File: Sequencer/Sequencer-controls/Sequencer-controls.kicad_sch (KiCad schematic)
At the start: 10 parts, among them SW1 SW_Push_DPDT, SW2 SW_Rotary3x4, SW3 SW_Rotary12

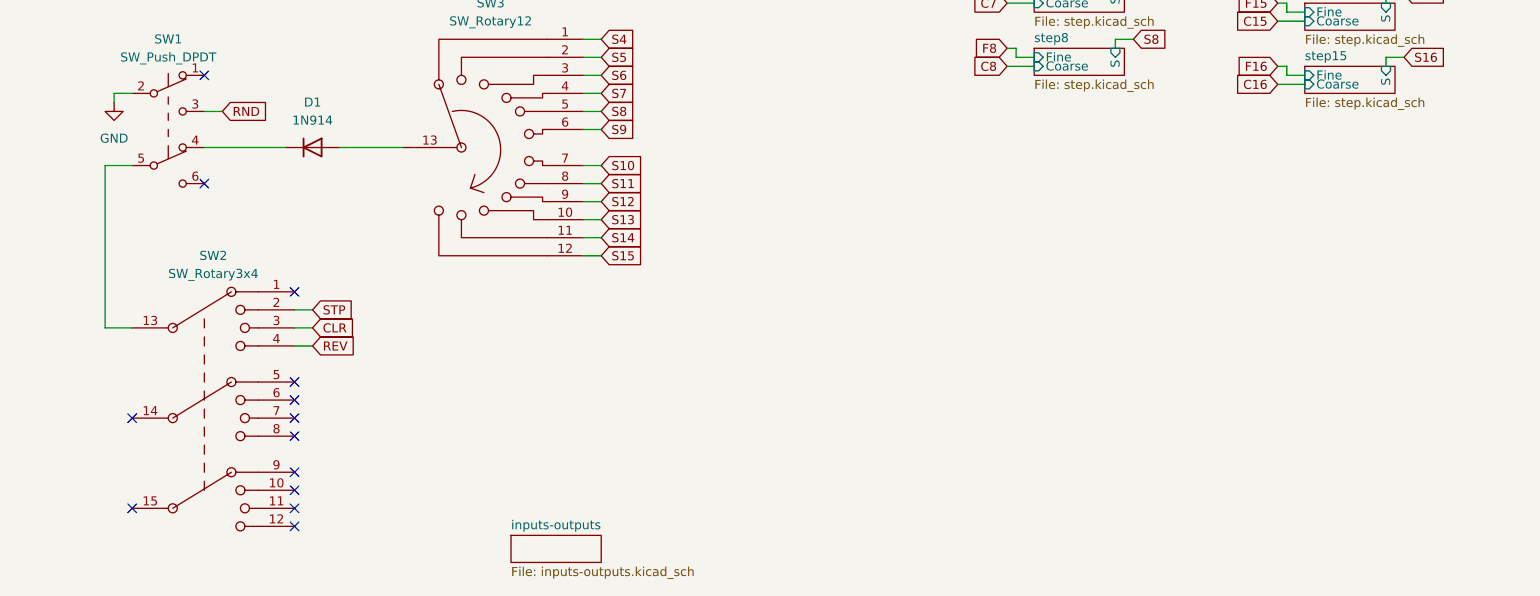
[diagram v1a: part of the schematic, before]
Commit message: adding connectors to sequencer
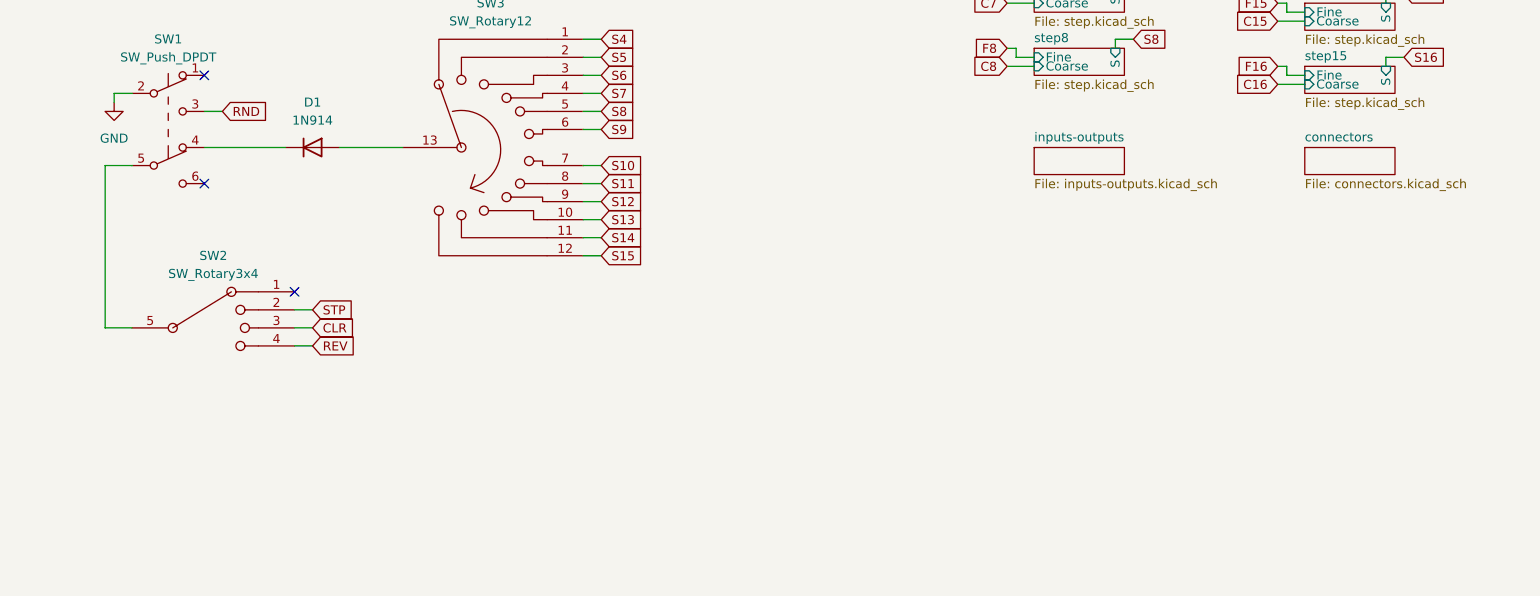
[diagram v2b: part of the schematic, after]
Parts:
- SW2: footprint (none) -> Library:rotary_switch_1P12T; symbol Switch:SW_Rotary3x4 -> Synth:SW_Rotary4
- SW3: footprint (none) -> Library:rotary_switch_1P12T
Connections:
- net at SW1.5 (B): now also SW2.5; no longer SW2.13
- no-connect marks 13 -> 3
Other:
- added sheet connectors (connectors.kicad_sch)
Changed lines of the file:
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@@
   )
   (no_connect (at 99.06 91.44))
-  (no_connect (at 88.9 139.7))
-  (no_connect (at 111.76 154.94))
-  (no_connect (at 88.9 152.4))
   (no_connect (at 111.76 121.92))
   (no_connect (at 99.06 106.68))
-  (no_connect (at 111.76 149.86))
-  (no_connect (at 111.76 142.24))
-  (no_connect (at 111.76 134.62))
-  (no_connect (at 111.76 139.7))
-  (no_connect (at 111.76 137.16))
-  (no_connect (at 111.76 152.4))
-  (no_connect (at 111.76 147.32))
   (wire (pts (xy 251.46 52.07) (xy 250.19 52.07))
     (stroke (width 0) (type default))
@@
       (effects (font (size 1.27 1.27)))
     )
-    (property "Footprint" "" (at 137.16 83.82 0)
+    (property "Footprint" "Library:rotary_switch_1P12T" (at 137.16 83.82 0)
       (effects (font (size 1.27 1.27)) hide)
     )
@@
     )
   )
-  (symbol (lib_id "Switch:SW_Rotary3x4") (at 99.06 139.7 0) (unit 1)
-    (in_bom yes) (on_board no) (dnp no) (fields_autoplaced)
+  (symbol (lib_id "Synth:SW_Rotary4") (at 99.06 127 0) (unit 1)
+    (in_bom yes) (on_board yes) (dnp no) (fields_autoplaced)
     (property "Reference" "SW2" (at 100.33 116.84 0)
       (effects (font (size 1.27 1.27)))
@@
       (effects (font (size 1.27 1.27)))
     )
-    (property "Footprint" "" (at 96.52 119.38 0)
+    (property "Footprint" "Library:rotary_switch_1P12T" (at 96.52 119.38 0)
       (effects (font (size 1.27 1.27)) hide)
     )
@@
     )
     (pin "1")
-    (pin "10")
-    (pin "11")
-    (pin "12")
-    (pin "13")
-    (pin "14")
-    (pin "15")
     (pin "2")
     (pin "3")
     (pin "4")
     (pin "5")
-    (pin "6")
-    (pin "7")
-    (pin "8")
-    (pin "9")
     (instances
       (project "Sequencer-controls"
@@
     )
   )
-  (sheet (at 142.24 156.21) (size 12.7 3.81) (fields_autoplaced)
+  (sheet (at 215.9 101.6) (size 12.7 3.81) (fields_autoplaced)
     (stroke (width 0.1524) (type solid))
     (fill (color 0 0 0 0.0000))
-    (property "Sheetname" "inputs-outputs" (at 142.24 155.4984 0)
+    (property "Sheetname" "inputs-outputs" (at 215.9 100.8884 0)
       (effects (font (size 1.27 1.27)) (justify left bottom))
     )
-    (property "Sheetfile" "inputs-outputs.kicad_sch" (at 142.24 160.6046 0)
+    (property "Sheetfile" "inputs-outputs.kicad_sch" (at 215.9 105.9946 0)
       (effects (font (size 1.27 1.27)) (justify left top))
     )
@@
       )
     )
+  )
+  (sheet (at 254 101.6) (size 12.7 3.81) (fields_autoplaced)
+    (stroke (width 0.1524) (type solid))
+    (fill (color 0 0 0 0.0000))
+    (property "Sheetname" "connectors" (at 254 100.8884 0)
+      (effects (font (size 1.27 1.27)) (justify left bottom))
+    )
+    (property "Sheetfile" "connectors.kicad_sch" (at 254 105.9946 0)
+      (effects (font (size 1.27 1.27)) (justify left top))
+    )
+    (instances
+      (project "Sequencer-controls"
+        (path "/0fe7de3d-0e02-4720-a37d-4e739d042412" (page "19"))
+      )
+    )

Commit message: Sequencer control fully routed
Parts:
- added H1, H2, H3: MountingHole_Pad, MountingHole:MountingHole_3.2mm_M3_Pad, symbol Mechanical:MountingHole_Pad
- SW2: footprint Library:rotary_switch_1P12T -> Library:rotary_switch_3P4T
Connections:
- net GND: now also H1.1, H2.1, H3.1
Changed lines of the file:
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@@
   (junction (at 101.6 38.1) (diameter 0) (color 0 0 0 0)
+  )
+  (junction (at 38.1 139.7) (diameter 0) (color 0 0 0 0)
+  )
+  (junction (at 38.1 127) (diameter 0) (color 0 0 0 0)
   )
   (junction (at 46.99 50.8) (diameter 0) (color 0 0 0 0)
@@
     (stroke (width 0) (type default))
   )
+  (wire (pts (xy 38.1 114.3) (xy 38.1 127))
+    (stroke (width 0) (type default))
+  )
   (wire (pts (xy 229.87 41.91) (xy 227.33 41.91))
     (stroke (width 0) (type default))
@@
     (stroke (width 0) (type default))
   )
+  (wire (pts (xy 29.21 139.7) (xy 38.1 139.7))
+    (stroke (width 0) (type default))
+  )
+  (wire (pts (xy 29.21 127) (xy 38.1 127))
+    (stroke (width 0) (type default))
+  )
   (wire (pts (xy 46.99 19.05) (xy 46.99 25.4))
     (stroke (width 0) (type default))
@@
     (stroke (width 0) (type default))
   )
+  (wire (pts (xy 29.21 114.3) (xy 38.1 114.3))
+    (stroke (width 0) (type default))
+  )
   (wire (pts (xy 99.06 63.5) (xy 101.6 63.5))
     (stroke (width 0) (type default))
@@
     (stroke (width 0) (type default))
   )
+  (wire (pts (xy 38.1 139.7) (xy 38.1 144.78))
+    (stroke (width 0) (type default))
+  )
   (wire (pts (xy 267.97 41.91) (xy 265.43 41.91))
     (stroke (width 0) (type default))
@@
     (stroke (width 0) (type default))
   )
+  (wire (pts (xy 38.1 127) (xy 38.1 139.7))
+    (stroke (width 0) (type default))
+  )
   (wire (pts (xy 250.19 74.93) (xy 254 74.93))
     (stroke (width 0) (type default))
@@
   (symbol (lib_id "power:+12V") (at 101.6 22.86 0) (unit 1)
     (in_bom yes) (on_board yes) (dnp no) (fields_autoplaced)
-    (property "Reference" "#PWR02" (at 101.6 26.67 0)
+    (property "Reference" "#PWR03" (at 101.6 26.67 0)
       (effects (font (size 1.27 1.27)) hide)
     )
@@
       (project "Sequencer-controls"
         (path "/0fe7de3d-0e02-4720-a37d-4e739d042412"
-          (reference "#PWR02") (unit 1)
+          (reference "#PWR03") (unit 1)
+        )
+      )
+    )
+  )
+  (symbol (lib_id "Mechanical:MountingHole_Pad") (at 26.67 127 90) (unit 1)
+    (in_bom yes) (on_board yes) (dnp no) (fields_autoplaced)
+    (property "Reference" "H2" (at 25.4 120.65 90)
+      (effects (font (size 1.27 1.27)))
+    )
+    (property "Value" "MountingHole_Pad" (at 25.4 123.19 90)
+      (effects (font (size 1.27 1.27)))
+    )
+    (property "Footprint" "MountingHole:MountingHole_3.2mm_M3_Pad" (at 26.67 127 0)
+      (effects (font (size 1.27 1.27)) hide)
+    )
+    (property "Datasheet" "~" (at 26.67 127 0)
+      (effects (font (size 1.27 1.27)) hide)
+    )
+    (pin "1")
+    (instances
+      (project "Sequencer-controls"
+        (path "/0fe7de3d-0e02-4720-a37d-4e739d042412"
+          (reference "H2") (unit 1)
         )
       )
@@
   (symbol (lib_id "power:GND") (at 86.36 95.25 0) (unit 1)
     (in_bom yes) (on_board yes) (dnp no) (fields_autoplaced)
-    (property "Reference" "#PWR01" (at 86.36 101.6 0)
+    (property "Reference" "#PWR02" (at 86.36 101.6 0)
       (effects (font (size 1.27 1.27)) hide)
     )
@@
       (project "Sequencer-controls"
         (path "/0fe7de3d-0e02-4720-a37d-4e739d042412"
-          (reference "#PWR01") (unit 1)
+          (reference "#PWR02") (unit 1)
         )
       )
@@
   (symbol (lib_id "power:GND") (at 101.6 67.31 0) (unit 1)
     (in_bom yes) (on_board yes) (dnp no) (fields_autoplaced)
-    (property "Reference" "#PWR03" (at 101.6 73.66 0)
+    (property "Reference" "#PWR04" (at 101.6 73.66 0)
       (effects (font (size 1.27 1.27)) hide)
     )
@@
       (project "Sequencer-controls"
         (path "/0fe7de3d-0e02-4720-a37d-4e739d042412"
-          (reference "#PWR03") (unit 1)
+          (reference "#PWR04") (unit 1)
         )
       )
@@
       (effects (font (size 1.27 1.27)))
     )
-    (property "Footprint" "Library:rotary_switch_1P12T" (at 96.52 119.38 0)
+    (property "Footprint" "Library:rotary_switch_3P4T" (at 96.52 119.38 0)
       (effects (font (size 1.27 1.27)) hide)
     )
@@
     )
   )
+  (symbol (lib_id "Mechanical:MountingHole_Pad") (at 26.67 114.3 90) (unit 1)
+    (in_bom yes) (on_board yes) (dnp no) (fields_autoplaced)
+    (property "Reference" "H1" (at 25.4 107.95 90)
+      (effects (font (size 1.27 1.27)))
+    )
+    (property "Value" "MountingHole_Pad" (at 25.4 110.49 90)
+      (effects (font (size 1.27 1.27)))
+    )
+    (property "Footprint" "MountingHole:MountingHole_3.2mm_M3_Pad" (at 26.67 114.3 0)
+      (effects (font (size 1.27 1.27)) hide)
+    )
+    (property "Datasheet" "~" (at 26.67 114.3 0)
+      (effects (font (size 1.27 1.27)) hide)
+    )
+    (pin "1")
+    (instances
+      (project "Sequencer-controls"
+        (path "/0fe7de3d-0e02-4720-a37d-4e739d042412"
+          (reference "H1") (unit 1)
+        )
+      )
+    )
+  )
   (symbol (lib_id "Device:R_Potentiometer") (at 41.91 50.8 270) (mirror x) (unit 1)
     (in_bom yes) (on_board yes) (dnp no)
@@
         (path "/a331be11-cf92-4101-a082-e20022c8dee2"
           (reference "RV1") (unit 1)
+        )
+      )
+    )
+  )
+  (symbol (lib_id "Mechanical:MountingHole_Pad") (at 26.67 139.7 90) (unit 1)
+    (in_bom yes) (on_board yes) (dnp no) (fields_autoplaced)
+    (property "Reference" "H3" (at 25.4 133.35 90)
+      (effects (font (size 1.27 1.27)))
+    )
+    (property "Value" "MountingHole_Pad" (at 25.4 135.89 90)
+      (effects (font (size 1.27 1.27)))
+    )
+    (property "Footprint" "MountingHole:MountingHole_3.2mm_M3_Pad" (at 26.67 139.7 0)
+      (effects (font (size 1.27 1.27)) hide)
+    )
+    (property "Datasheet" "~" (at 26.67 139.7 0)
+      (effects (font (size 1.27 1.27)) hide)
+    )
+    (pin "1")
+    (instances
+      (project "Sequencer-controls"
+        (path "/0fe7de3d-0e02-4720-a37d-4e739d042412"
+          (reference "H3") (unit 1)
         )
       )
@@
         )
       )
+    )
+  )
+  (symbol (lib_id "power:GND") (at 38.1 144.78 0) (unit 1)
+    (in_bom yes) (on_board yes) (dnp no) (fields_autoplaced)
+    (property "Reference" "#PWR01" (at 38.1 151.13 0)
+      (effects (font (size 1.27 1.27)) hide)
+    )
+    (property "Value" "GND" (at 38.1 149.86 0)
+      (effects (font (size 1.27 1.27)))
+    )
+    (property "Footprint" "" (at 38.1 144.78 0)
+      (effects (font (size 1.27 1.27)) hide)
+    )
+    (property "Datasheet" "" (at 38.1 144.78 0)
+      (effects (font (size 1.27 1.27)) hide)
+    )
+    (pin "1")
+    (instances
+      (project "Sequencer-controls"
+        (path "/0fe7de3d-0e02-4720-a37d-4e739d042412"
+          (reference "#PWR01") (unit 1)
+        )
+      )

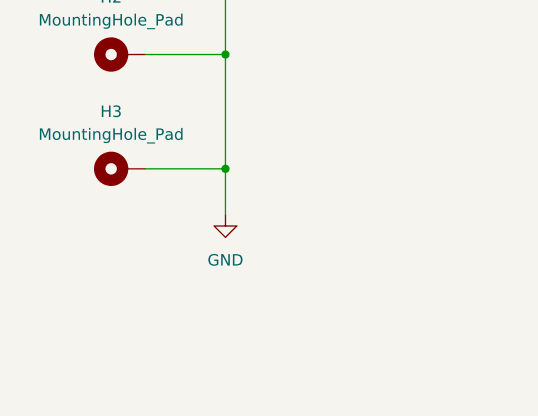
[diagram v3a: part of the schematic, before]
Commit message: moved to 4 layers
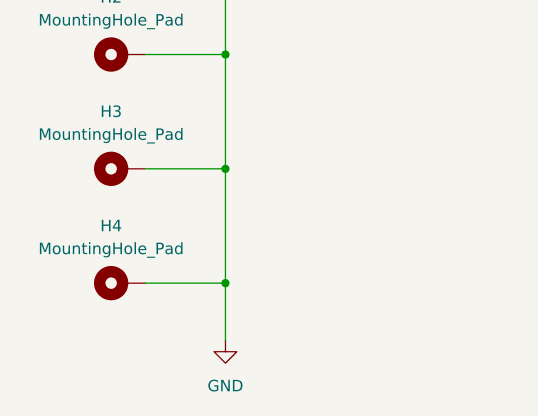
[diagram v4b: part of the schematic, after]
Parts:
- added H4: MountingHole_Pad, MountingHole:MountingHole_3.2mm_M3_Pad, symbol Mechanical:MountingHole_Pad
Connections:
- net GND: now also H4.1
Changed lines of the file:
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@@
   (junction (at 38.1 127) (diameter 0) (color 0 0 0 0)
+  )
+  (junction (at 38.1 152.4) (diameter 0) (color 0 0 0 0)
   )
   (junction (at 46.99 50.8) (diameter 0) (color 0 0 0 0)
@@
     (stroke (width 0) (type default))
   )
+  (wire (pts (xy 38.1 152.4) (xy 38.1 158.75))
+    (stroke (width 0) (type default))
+  )
   (wire (pts (xy 88.9 93.98) (xy 86.36 93.98))
     (stroke (width 0) (type default))
@@
     (stroke (width 0) (type default))
   )
+  (wire (pts (xy 29.21 152.4) (xy 38.1 152.4))
+    (stroke (width 0) (type default))
+  )
   (wire (pts (xy 227.33 24.13) (xy 227.33 25.4))
     (stroke (width 0) (type default))
@@
     (stroke (width 0) (type default))
   )
-  (wire (pts (xy 38.1 139.7) (xy 38.1 144.78))
+  (wire (pts (xy 38.1 139.7) (xy 38.1 152.4))
     (stroke (width 0) (type default))
   )
@@
     )
   )
+  (symbol (lib_id "Mechanical:MountingHole_Pad") (at 26.67 152.4 90) (unit 1)
+    (in_bom yes) (on_board yes) (dnp no) (fields_autoplaced)
+    (property "Reference" "H4" (at 25.4 146.05 90)
+      (effects (font (size 1.27 1.27)))
+    )
+    (property "Value" "MountingHole_Pad" (at 25.4 148.59 90)
+      (effects (font (size 1.27 1.27)))
+    )
+    (property "Footprint" "MountingHole:MountingHole_3.2mm_M3_Pad" (at 26.67 152.4 0)
+      (effects (font (size 1.27 1.27)) hide)
+    )
+    (property "Datasheet" "~" (at 26.67 152.4 0)
+      (effects (font (size 1.27 1.27)) hide)
+    )
+    (pin "1")
+    (instances
+      (project "Sequencer-controls"
+        (path "/0fe7de3d-0e02-4720-a37d-4e739d042412"
+          (reference "H4") (unit 1)
+        )
+      )
+    )
+  )
   (symbol (lib_id "power:GND") (at 86.36 95.25 0) (unit 1)
     (in_bom yes) (on_board yes) (dnp no) (fields_autoplaced)
@@
     )
   )
-  (symbol (lib_id "power:GND") (at 38.1 144.78 0) (unit 1)
-    (in_bom yes) (on_board yes) (dnp no) (fields_autoplaced)
-    (property "Reference" "#PWR01" (at 38.1 151.13 0)
-      (effects (font (size 1.27 1.27)) hide)
-    )
-    (property "Value" "GND" (at 38.1 149.86 0)
-      (effects (font (size 1.27 1.27)))
-    )
-    (property "Footprint" "" (at 38.1 144.78 0)
-      (effects (font (size 1.27 1.27)) hide)
-    )
-    (property "Datasheet" "" (at 38.1 144.78 0)
-      (effects (font (size 1.27 1.27)) hide)
-    )
+  (symbol (lib_id "power:GND") (at 38.1 158.75 0) (unit 1)
+    (in_bom yes) (on_board yes) (dnp no) (fields_autoplaced)
+    (property "Reference" "#PWR01" (at 38.1 165.1 0)
+      (effects (font (size 1.27 1.27)) hide)
+    )
+    (property "Value" "GND" (at 38.1 163.83 0)
+      (effects (font (size 1.27 1.27)))
+    )
+    (property "Footprint" "" (at 38.1 158.75 0)
+      (effects (font (size 1.27 1.27)) hide)
+    )
+    (property "Datasheet" "" (at 38.1 158.75 0)
+      (effects (font (size 1.27 1.27)) hide)
+    )

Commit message: misc
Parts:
- PORTAMENTO1, RATE1: symbol Device:R_Potentiometer -> Device:R_Potentiometer_MountingPin
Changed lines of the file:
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@@
     )
   )
-  (symbol (lib_id "Device:R_Potentiometer") (at 41.91 50.8 270) (mirror x) (unit 1)
+  (symbol (lib_id "Device:R_Potentiometer_MountingPin") (at 41.91 50.8 270) (mirror x) (unit 1)
     (in_bom yes) (on_board yes) (dnp no)
     (property "Reference" "RATE1" (at 43.18 53.34 0)
@@
     (pin "2")
     (pin "3")
+    (pin "MP")
     (instances
       (project "Sequencer-controls"
@@
     )
   )
-  (symbol (lib_id "Device:R_Potentiometer") (at 41.91 25.4 270) (mirror x) (unit 1)
+  (symbol (lib_id "Device:R_Potentiometer_MountingPin") (at 41.91 25.4 270) (mirror x) (unit 1)
     (in_bom yes) (on_board yes) (dnp no)
     (property "Reference" "PORTAMENTO1" (at 43.18 27.94 0)
@@
     (pin "2")
     (pin "3")
+    (pin "MP")
     (instances
       (project "Sequencer-controls"

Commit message: Sequencer control - minor
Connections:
- net GND: now also PORTAMENTO1.MP (MountPin), RATE1.MP (MountPin)
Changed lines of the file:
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@@
+    (stroke (width 0) (type default))
+  )
+  (wire (pts (xy 41.91 55.88) (xy 41.91 58.42))
     (stroke (width 0) (type default))
   )
@@
     (stroke (width 0) (type default))
   )
+  (wire (pts (xy 41.91 30.48) (xy 41.91 33.02))
+    (stroke (width 0) (type default))
+  )
   (wire (pts (xy 46.99 44.45) (xy 46.99 50.8))
     (stroke (width 0) (type default))
@@
         (path "/0fe7de3d-0e02-4720-a37d-4e739d042412"
           (reference "#PWR03") (unit 1)
+        )
+      )
+    )
+  )
+  (symbol (lib_id "power:GND") (at 41.91 33.02 0) (unit 1)
+    (in_bom yes) (on_board yes) (dnp no) (fields_autoplaced)
+    (property "Reference" "#PWR079" (at 41.91 39.37 0)
+      (effects (font (size 1.27 1.27)) hide)
+    )
+    (property "Value" "GND" (at 41.91 38.1 0)
+      (effects (font (size 1.27 1.27)))
+    )
+    (property "Footprint" "" (at 41.91 33.02 0)
+      (effects (font (size 1.27 1.27)) hide)
+    )
+    (property "Datasheet" "" (at 41.91 33.02 0)
+      (effects (font (size 1.27 1.27)) hide)
+    )
+    (pin "1")
+    (instances
+      (project "Sequencer-controls"
+        (path "/0fe7de3d-0e02-4720-a37d-4e739d042412"
+          (reference "#PWR079") (unit 1)
         )
       )
@@
         )
       )
+    )
+  )
+  (symbol (lib_id "power:GND") (at 41.91 58.42 0) (unit 1)
+    (in_bom yes) (on_board yes) (dnp no) (fields_autoplaced)
+    (property "Reference" "#PWR078" (at 41.91 64.77 0)
+      (effects (font (size 1.27 1.27)) hide)
+    )
+    (property "Value" "GND" (at 41.91 63.5 0)
+      (effects (font (size 1.27 1.27)))
+    )
+    (property "Footprint" "" (at 41.91 58.42 0)
+      (effects (font (size 1.27 1.27)) hide)
+    )
+    (property "Datasheet" "" (at 41.91 58.42 0)
+      (effects (font (size 1.27 1.27)) hide)
+    )
+    (pin "1")
+    (instances
+      (project "Sequencer-controls"
+        (path "/0fe7de3d-0e02-4720-a37d-4e739d042412"
+          (reference "#PWR078") (unit 1)
+        )
+      )
